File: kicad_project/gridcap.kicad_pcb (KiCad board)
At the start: 2 copper layers, 119.1 x 108.7 mm, 69 parts, among them J1 Conn_01x10

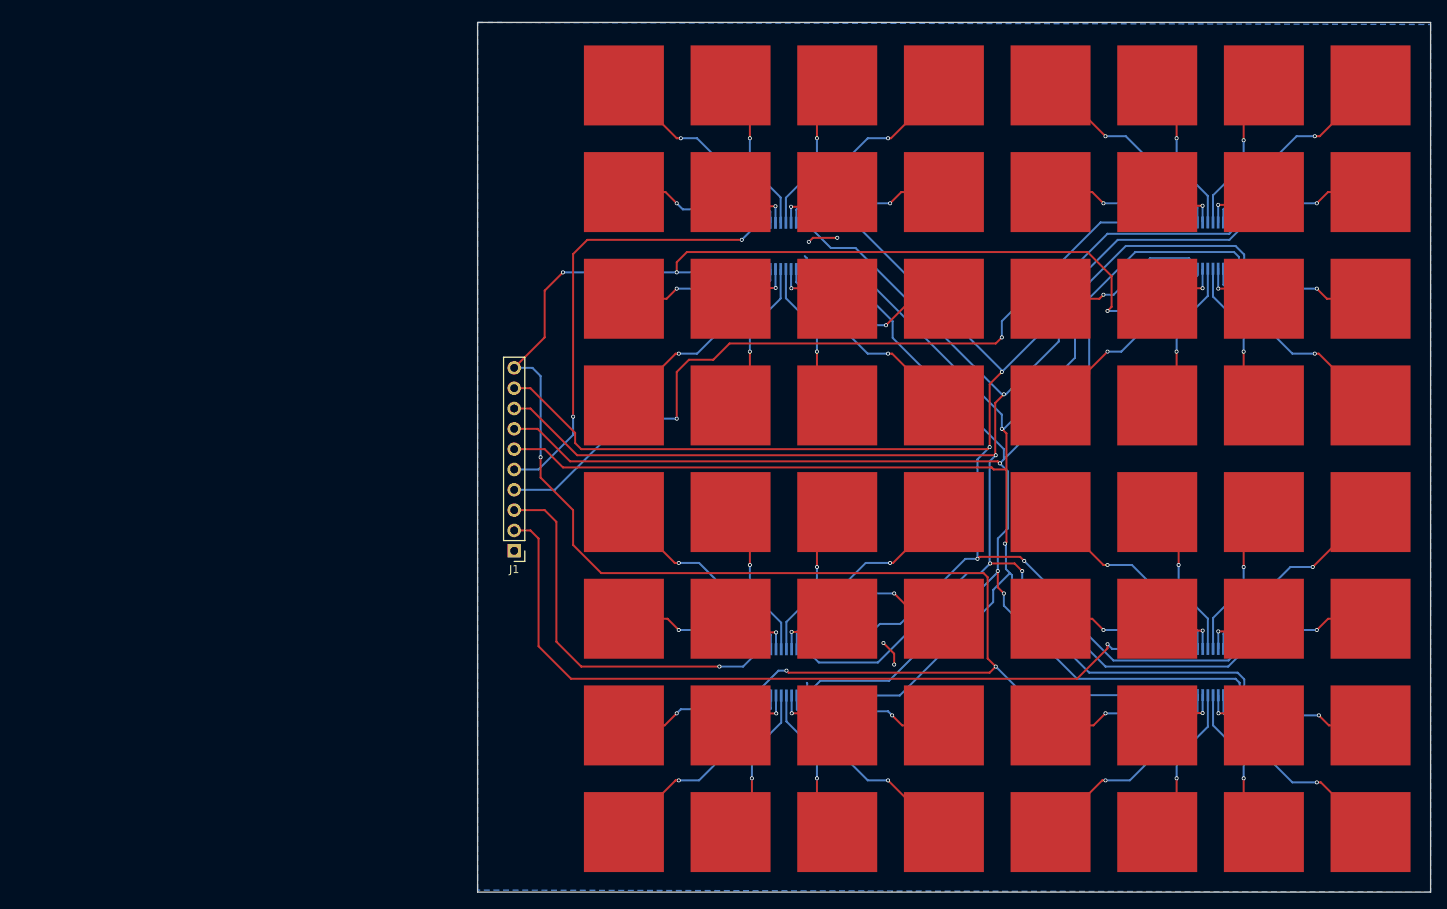
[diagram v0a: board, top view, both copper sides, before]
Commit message: Fix pcb design to fit cogra limitations
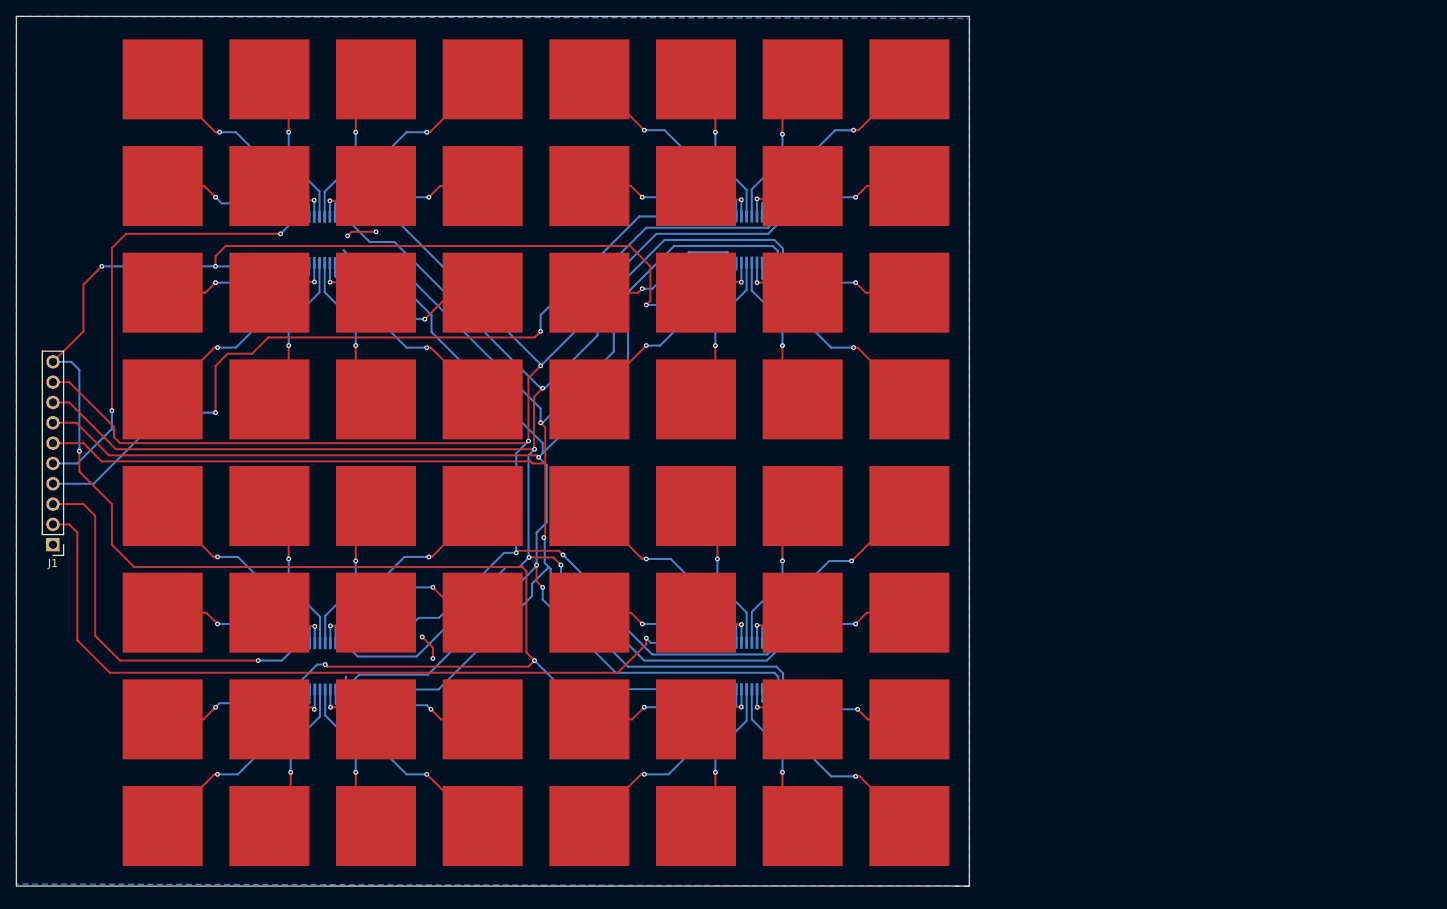
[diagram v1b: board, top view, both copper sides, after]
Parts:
- moved MUX1 57.7 mm to (128.0, 72.7)
- moved MUX2 57.7 mm to (181.4, 72.6)
- moved MUX3 57.7 mm to (128.1, 126.0)
- moved MUX4 57.7 mm to (181.4, 125.9)
- moved PAD15 57.7 mm to (187.4, 65.9)
- moved PAD23 57.7 mm to (187.4, 79.3)
- moved PAD31 57.7 mm to (187.4, 92.6)
- moved PAD39 57.7 mm to (187.4, 105.9)
- moved PAD47 57.7 mm to (187.4, 119.3)
- moved PAD55 57.7 mm to (187.4, 132.6)
- moved PAD63 57.7 mm to (187.4, 145.9)
- moved PAD7 57.7 mm to (187.4, 52.6)
- moved J1 57.7 mm to (93.7, 110.8)
- moved PAD1 57.7 mm to (107.5, 52.6)
- moved PAD10 57.7 mm to (120.8, 65.9)
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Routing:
- net Vcc: track 262.0 -> 262.7 mm

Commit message: Change to fit aisler limitations and add plugin for aisler
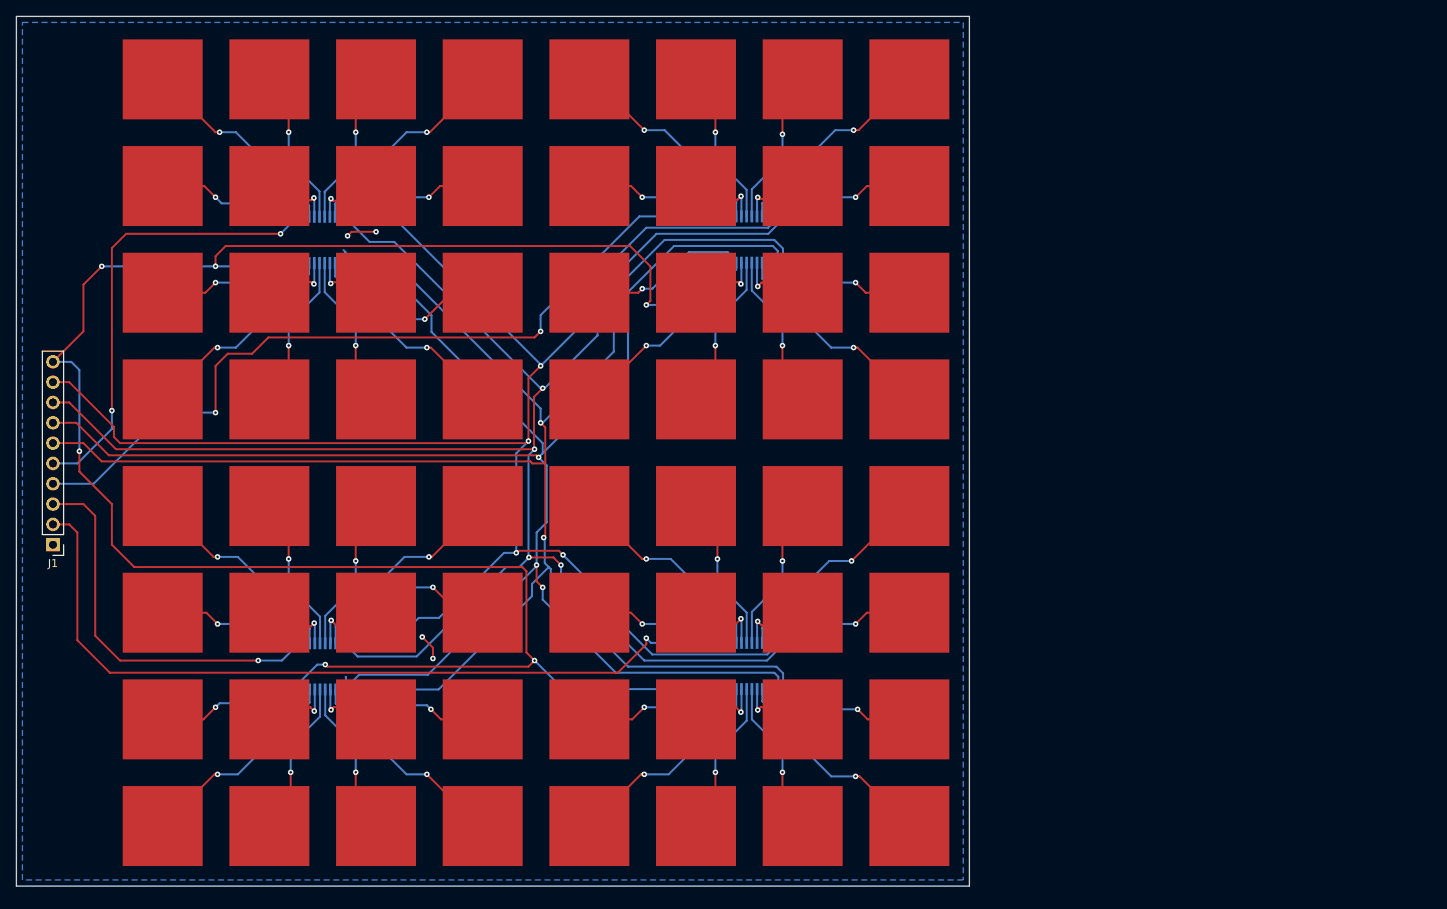
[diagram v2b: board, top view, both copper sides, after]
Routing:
- net Net-(MUX4-Y5): track 8.58 -> 9.57 mm
- net Net-(MUX3-Y2): track 8.56 -> 9.47 mm
- net Net-(MUX4-Y10): track 8.55 -> 9.43 mm
- net Net-(MUX4-Y2): track 8.55 -> 9.20 mm
- net Net-(MUX2-Y13): track 8.72 -> 9.35 mm
- net Net-(MUX2-Y5): track 8.47 -> 9.07 mm
- net Net-(MUX3-Y5): track 8.51 -> 9.03 mm
